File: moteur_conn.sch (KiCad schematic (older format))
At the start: 1 part, among them J12 Moteur

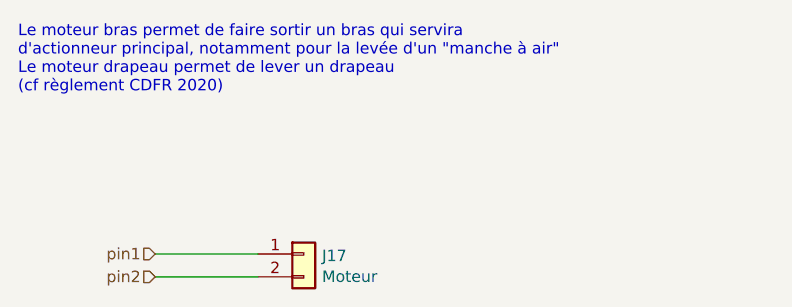
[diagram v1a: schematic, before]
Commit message: removed psi-things pins, added transceiver MCP2551 for CAN, changed motors input protocol, RS must be chosen 1 or 10 kohms, and a foot print for a potentitial 120 ohms resistor is present for CAN bus end.
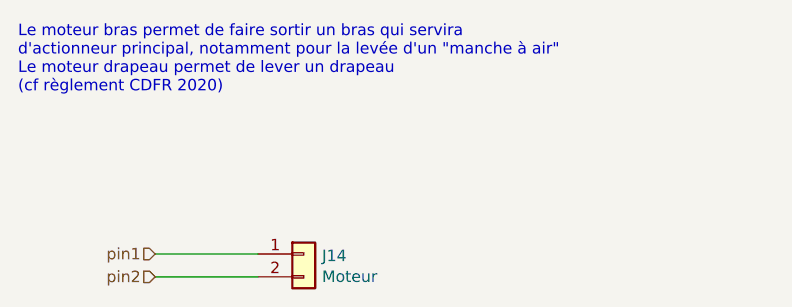
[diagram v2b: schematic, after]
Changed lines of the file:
@@
 $Descr A4 11693 8268
 encoding utf-8
-Sheet 20 24
+Sheet 18 23
 Title ""
 Date ""
@@
 AR Path="/5E685B22/5E6C3064" Ref="J12"  Part="1"
 AR Path="/5E685A03/5E6C3064" Ref="J11"  Part="1"
-AR Path="/5F8AAE69/5E6C3064" Ref="J17"  Part="1"
-F 0 "J17" H 5530 2592 50  0000 L CNN
+AR Path="/5F8AAE69/5E6C3064" Ref="J14"  Part="1"
+F 0 "J14" H 5530 2592 50  0000 L CNN
 F 1 "Moteur" H 5530 2501 50  0000 L CNN
 F 2 "Connector_JST:JST_PH_B2B-PH-K_1x02_P2.00mm_Vertical" H 5450 2600 50  0001 C CNN

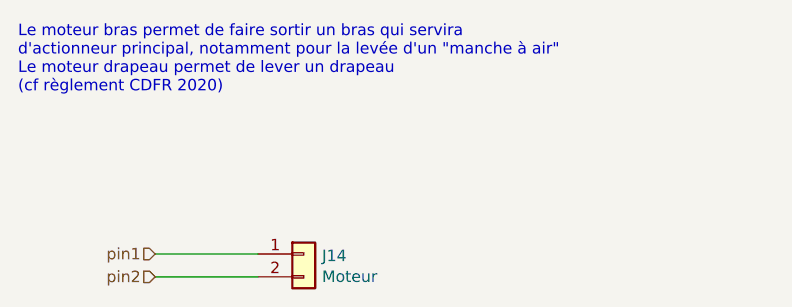
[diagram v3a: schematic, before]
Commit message: correction mm -> inch, empreinte du bouton
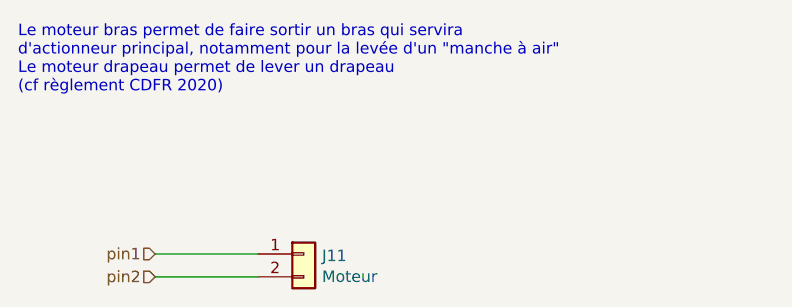
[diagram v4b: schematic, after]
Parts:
- J12: footprint Connector_JST:JST_PH_B2B-PH-K_1x02_P2.00mm_Vertical -> Connector_JST:JST_XH_B2B-XH-A_1x02_P2.50mm_Vertical
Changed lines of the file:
@@
 AR Path="/5E685A03/5E6C3064" Ref="J11"  Part="1"
 AR Path="/5F8AAE69/5E6C3064" Ref="J14"  Part="1"
-F 0 "J14" H 5530 2592 50  0000 L CNN
+F 0 "J11" H 5530 2592 50  0000 L CNN
 F 1 "Moteur" H 5530 2501 50  0000 L CNN
-F 2 "Connector_JST:JST_PH_B2B-PH-K_1x02_P2.00mm_Vertical" H 5450 2600 50  0001 C CNN
+F 2 "Connector_JST:JST_XH_B2B-XH-A_1x02_P2.50mm_Vertical" H 5450 2600 50  0001 C CNN
 F 3 "~" H 5450 2600 50  0001 C CNN
 	1    5450 2600
